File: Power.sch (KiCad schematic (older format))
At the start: 1 part

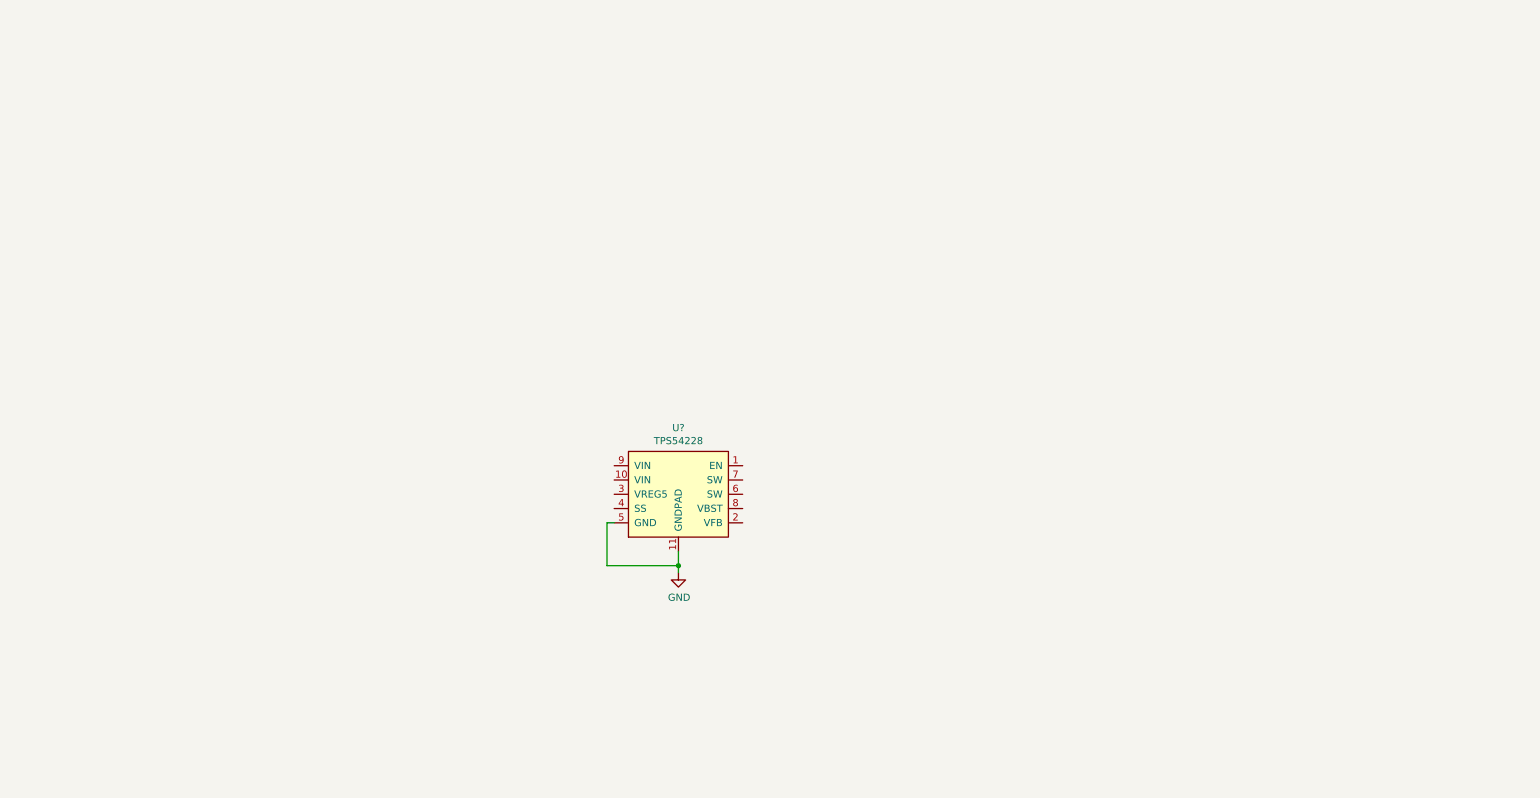
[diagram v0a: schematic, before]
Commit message: Draw power schematic
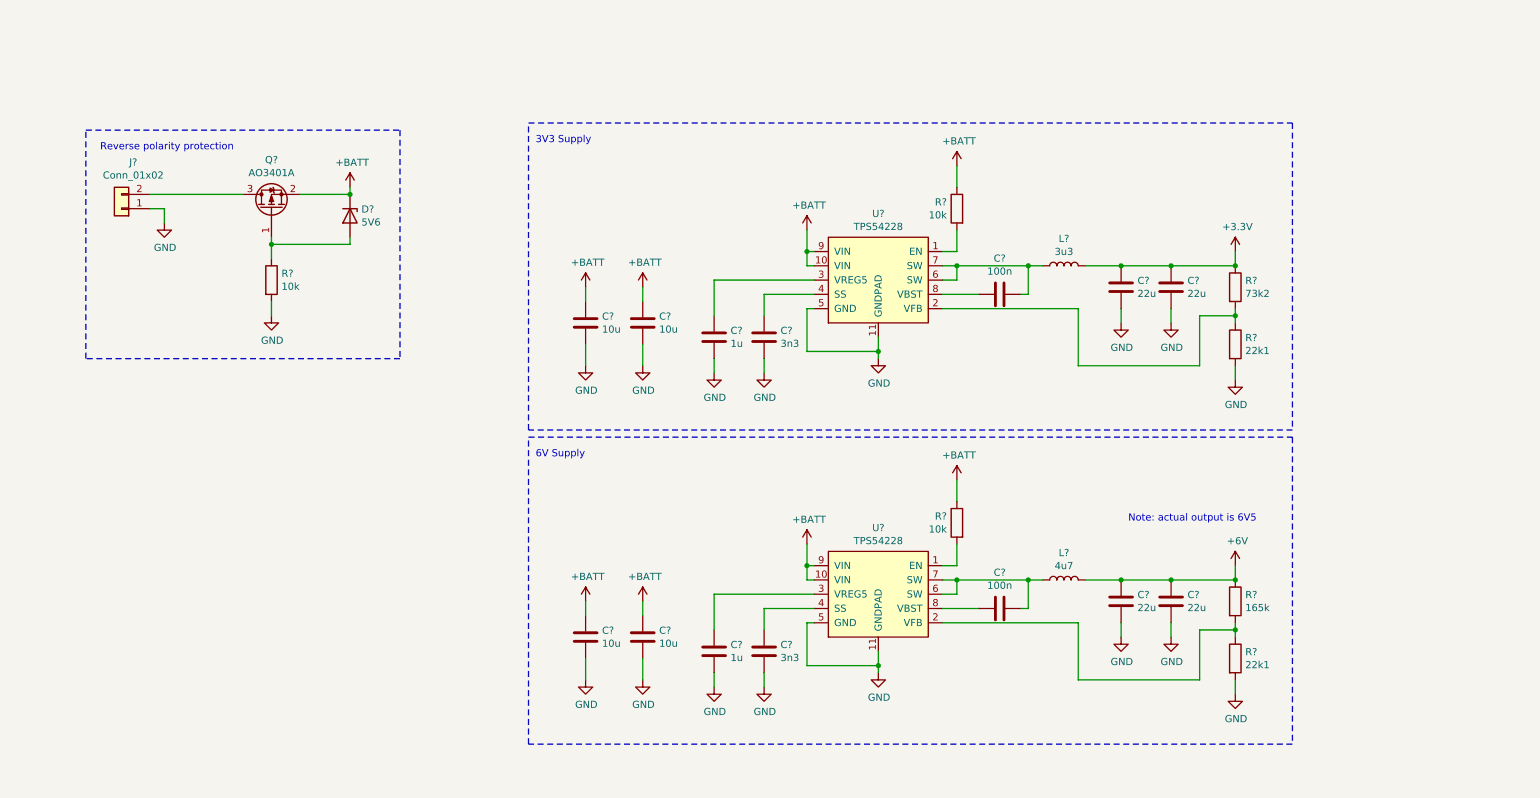
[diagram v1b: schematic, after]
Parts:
- added C? (x2): 1u, symbol Device:C
- added C? (x2): 3n3, symbol Device:C
- added C? (x2): 100n, symbol Device:C
- added C? (x4): 10u, symbol Device:C
- added C? (x4): 22u, symbol Device:C
- added D?: 5V6, symbol Device:D_Zener
- added J?: Conn_01x02, symbol Connector_Generic:Conn_01x02
- added L?: 3u3, symbol Device:L
- added L?: 4u7, symbol Device:L
- added Q?: AO3401A, Package_TO_SOT_SMD:SOT-23, symbol Transistor_FET:AO3401A
- added R? (x3): 10k, symbol Device:R
- added R?: 73k2, symbol Device:R
- added R? (x2): 22k1, symbol Device:R
- added R?: 165k, symbol Device:R
- added U?: TPS54228, symbol co2_sensor_node:TPS54228
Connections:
- net GND: now also C?.2, C?.2, C?.2, C?.2, C?.2, C?.2, C?.2, C?.2, C?.2, C?.2, C?.2, C?.2, J?.1 (Pin_1), R?.2, R?.2, R?.2, U?.11 (GNDPAD), U?.5 (GND)
- net at U?.1 (EN): now also R?.2
- net +BATT: now reaches U?.10 (VIN)
- net +BATT: now also U?.9 (VIN), C?.1, C?.1, C?.1, C?.1, D?.1 (K), Q?.2 (S), R?.1, R?.1, U?.10 (VIN), U?.9 (VIN)
- net at U?.2 (VFB): now also R?.1, R?.2
- net at U?.3 (VREG5): now also C?.1
- net at U?.4 (SS): now also C?.1
- net at U?.6 (SW): now also U?.7 (SW), C?.1, L?.1
- net at U?.8 (VBST): now also C?.2
- new net: R?.2, U?.1 (EN)
- new net: R?.1, R?.2, U?.2 (VFB)
- new net: C?.1, U?.3 (VREG5)
- new net: C?.1, U?.4 (SS)
- new net: C?.1, L?.1, U?.6 (SW), U?.7 (SW)
- new net: C?.2, U?.8 (VBST)
- new net: D?.2 (A), Q?.1 (G), R?.1
- new net: J?.2 (Pin_2), Q?.3 (D)
- new net +3V3: C?.1, C?.1, L?.2, R?.1
- new net +6V: C?.1, C?.1, L?.2, R?.1
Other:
- note added: "3V3 Supply\n"
- note added: "6V Supply\n"
- note added: "Note: actual output is 6V5\n"
- note added: "Reverse polarity protection"
- moved on the sheet: U?

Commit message: Change BME280 out for connector
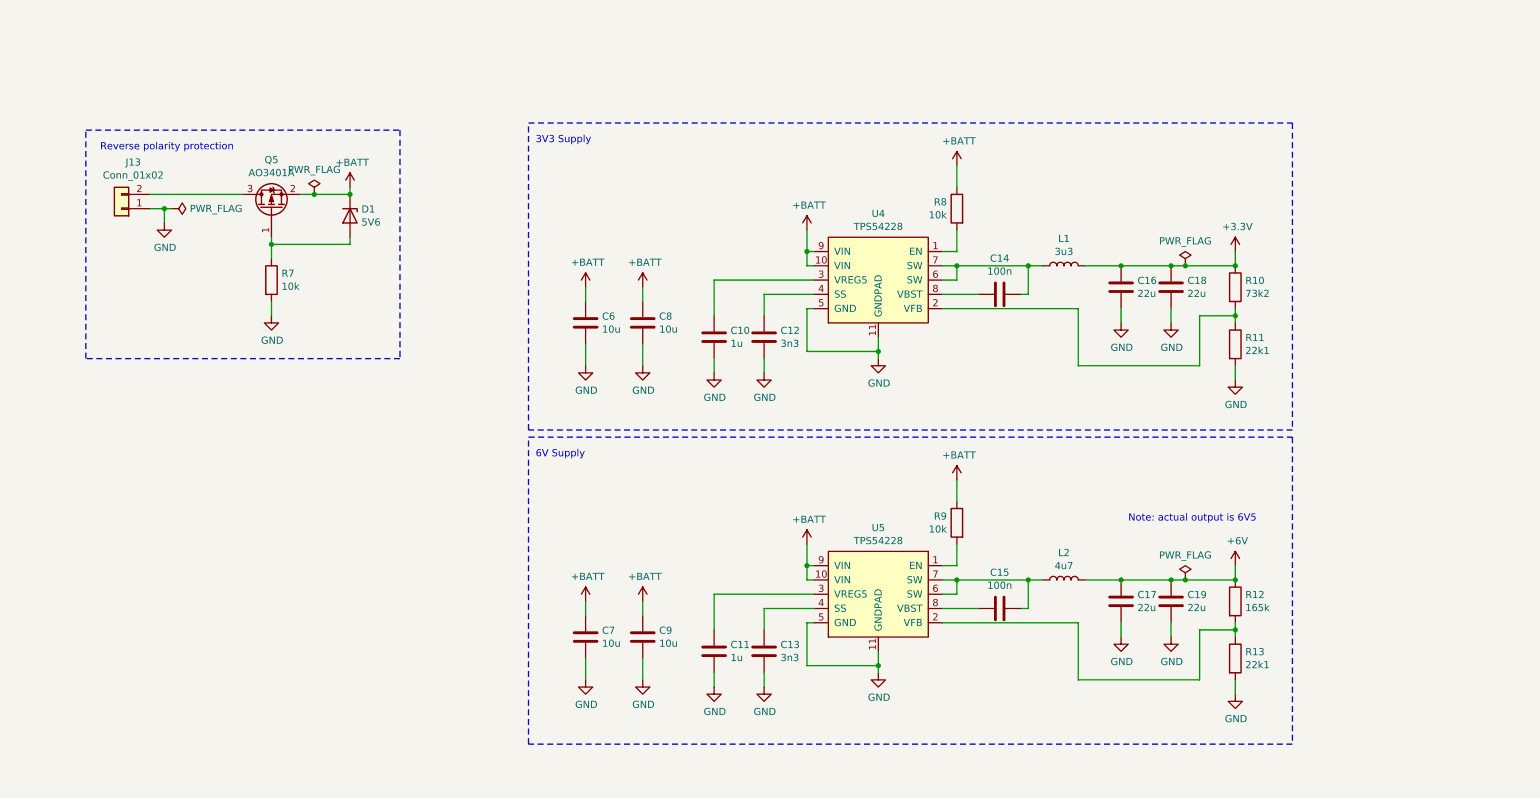
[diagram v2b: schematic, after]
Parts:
- gave numbers to parts that had none: 28

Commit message: Begin assigning footprints
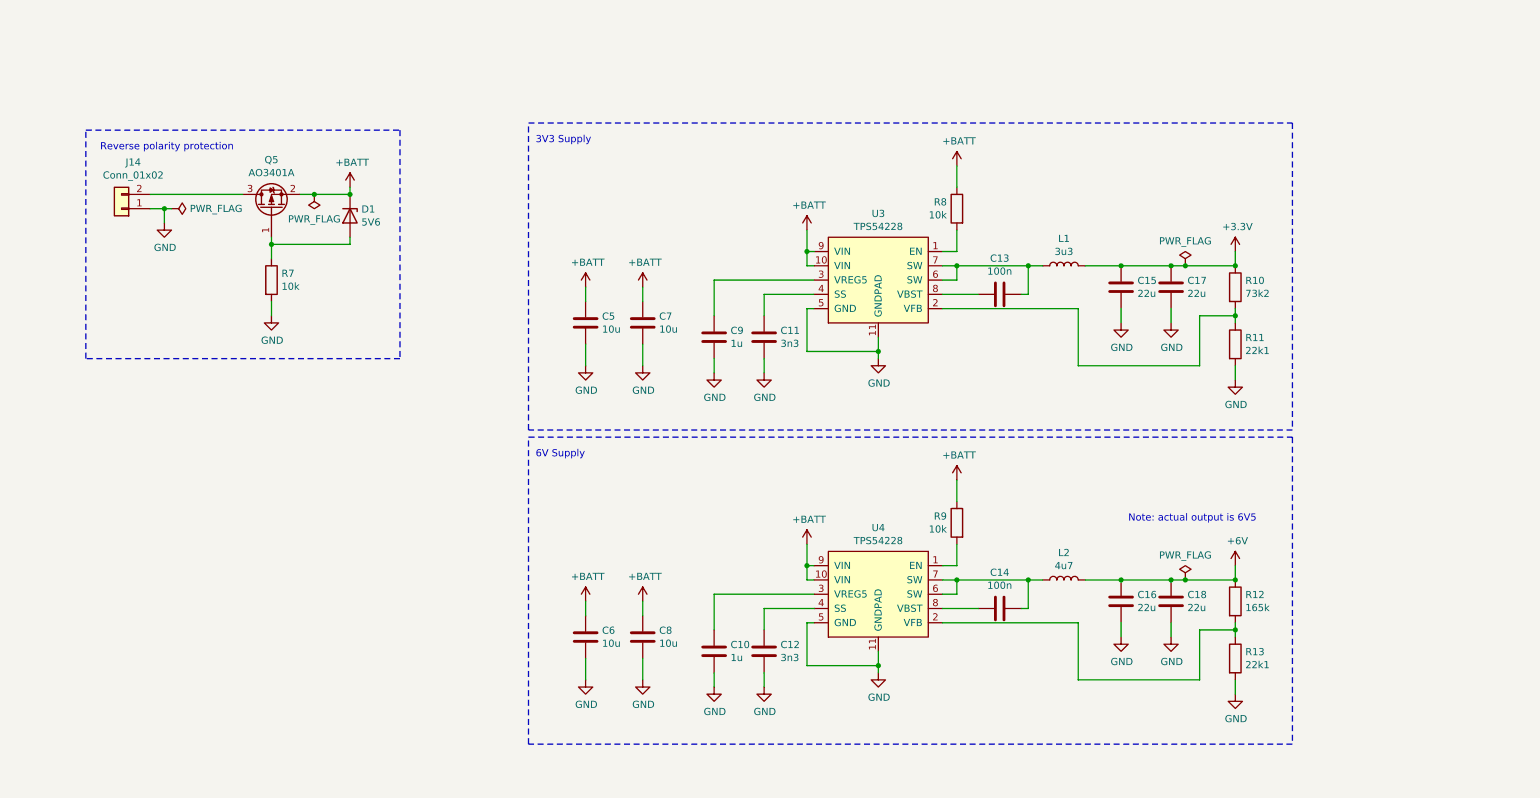
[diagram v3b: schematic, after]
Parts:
- C10: renamed from C11; footprint (none) -> Capacitor_SMD:C_0603_1608Metric; LCSC (none) -> C15849
- C11: renamed from C12; footprint (none) -> Capacitor_SMD:C_0603_1608Metric; LCSC (none) -> C1613
- C12: renamed from C13; footprint (none) -> Capacitor_SMD:C_0603_1608Metric; LCSC (none) -> C1613
- C13: renamed from C14; footprint (none) -> Capacitor_SMD:C_0603_1608Metric; LCSC (none) -> C14663
- C14: renamed from C15; footprint (none) -> Capacitor_SMD:C_0603_1608Metric; LCSC (none) -> C14663
- C15: renamed from C16; footprint (none) -> Capacitor_SMD:C_0805_2012Metric
- C16: renamed from C17; footprint (none) -> Capacitor_SMD:C_0805_2012Metric
- C17: renamed from C18; footprint (none) -> Capacitor_SMD:C_0805_2012Metric
- C18: renamed from C19; footprint (none) -> Capacitor_SMD:C_0805_2012Metric
- C5: renamed from C6; footprint (none) -> Capacitor_SMD:C_0805_2012Metric
- C6: renamed from C7; footprint (none) -> Capacitor_SMD:C_0805_2012Metric
- C7: renamed from C8; footprint (none) -> Capacitor_SMD:C_0805_2012Metric
- C8: renamed from C9; footprint (none) -> Capacitor_SMD:C_0805_2012Metric
- C9: renamed from C10; footprint (none) -> Capacitor_SMD:C_0603_1608Metric; LCSC (none) -> C15849
- D1: footprint (none) -> Diode_SMD:D_MiniMELF
- Q5: LCSC (none) -> C15127
- R10: footprint (none) -> Resistor_SMD:R_0603_1608Metric; LCSC (none) -> C14890
- R11, R13: footprint (none) -> Resistor_SMD:R_0603_1608Metric; LCSC (none) -> C25961
- R12: footprint (none) -> Resistor_SMD:R_0603_1608Metric; LCSC (none) -> C22816
- R7, R8, R9: footprint (none) -> Resistor_SMD:R_0603_1608Metric; LCSC (none) -> C25804
- renumbered J13 to J14, U4 to U3, U5 to U4

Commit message: Finish attaching footprints for revision 1
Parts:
- J14: footprint (none) -> Connector_JST:JST_XH_B2B-XH-AM_1x02_P2.50mm_Vertical
- L1: footprint (none) -> co2_sensor_node:YP0403
- L2: footprint (none) -> co2_sensor_node:WPN4020
- U3, U4: footprint (none) -> Package_SO:SOIC-8_3.9x4.9mm_P1.27mm
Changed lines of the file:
@@
 F 0 "U3" H 6750 3365 50  0000 C CNN
 F 1 "TPS54228" H 6750 3274 50  0000 C CNN
-F 2 "" H 6750 3350 50  0001 C CNN
+F 2 "Package_SO:SOIC-8_3.9x4.9mm_P1.27mm" H 6750 3350 50  0001 C CNN
 F 3 "" H 6750 3350 50  0001 C CNN
 	1    6900 2600
@@
 F 0 "L1" V 8240 2200 50  0000 C CNN
 F 1 "3u3" V 8149 2200 50  0000 C CNN
-F 2 "" H 8050 2200 50  0001 C CNN
-F 3 "~" H 8050 2200 50  0001 C CNN
+F 2 "co2_sensor_node:YP0403" H 8050 2200 50  0001 C CNN
+F 3 "~" H 8050 2200 50  0001 C CIN
 F 4 "C492275" V 8050 2200 50  0001 C CNN "LCSC"
 	1    8050 2200
@@
 F 0 "U4" H 6750 5565 50  0000 C CNN
 F 1 "TPS54228" H 6750 5474 50  0000 C CNN
-F 2 "" H 6750 5550 50  0001 C CNN
+F 2 "Package_SO:SOIC-8_3.9x4.9mm_P1.27mm" H 6750 5550 50  0001 C CNN
 F 3 "" H 6750 5550 50  0001 C CNN
 	1    6900 4800
@@
 F 0 "L2" V 8240 4400 50  0000 C CNN
 F 1 "4u7" V 8149 4400 50  0000 C CNN
-F 2 "" H 8050 4400 50  0001 C CNN
+F 2 "co2_sensor_node:WPN4020" H 8050 4400 50  0001 C CNN
 F 3 "~" H 8050 4400 50  0001 C CNN
 F 4 "C98363" V 8050 4400 50  0001 C CNN "LCSC"
@@
 F 0 "J14" H 1368 1475 50  0000 C CNN
 F 1 "Conn_01x02" H 1368 1566 50  0000 C CNN
-F 2 "" H 1450 1800 50  0001 C CNN
+F 2 "Connector_JST:JST_XH_B2B-XH-AM_1x02_P2.50mm_Vertical" H 1450 1800 50  0001 C CNN
 F 3 "~" H 1450 1800 50  0001 C CNN
 	1    1450 1800

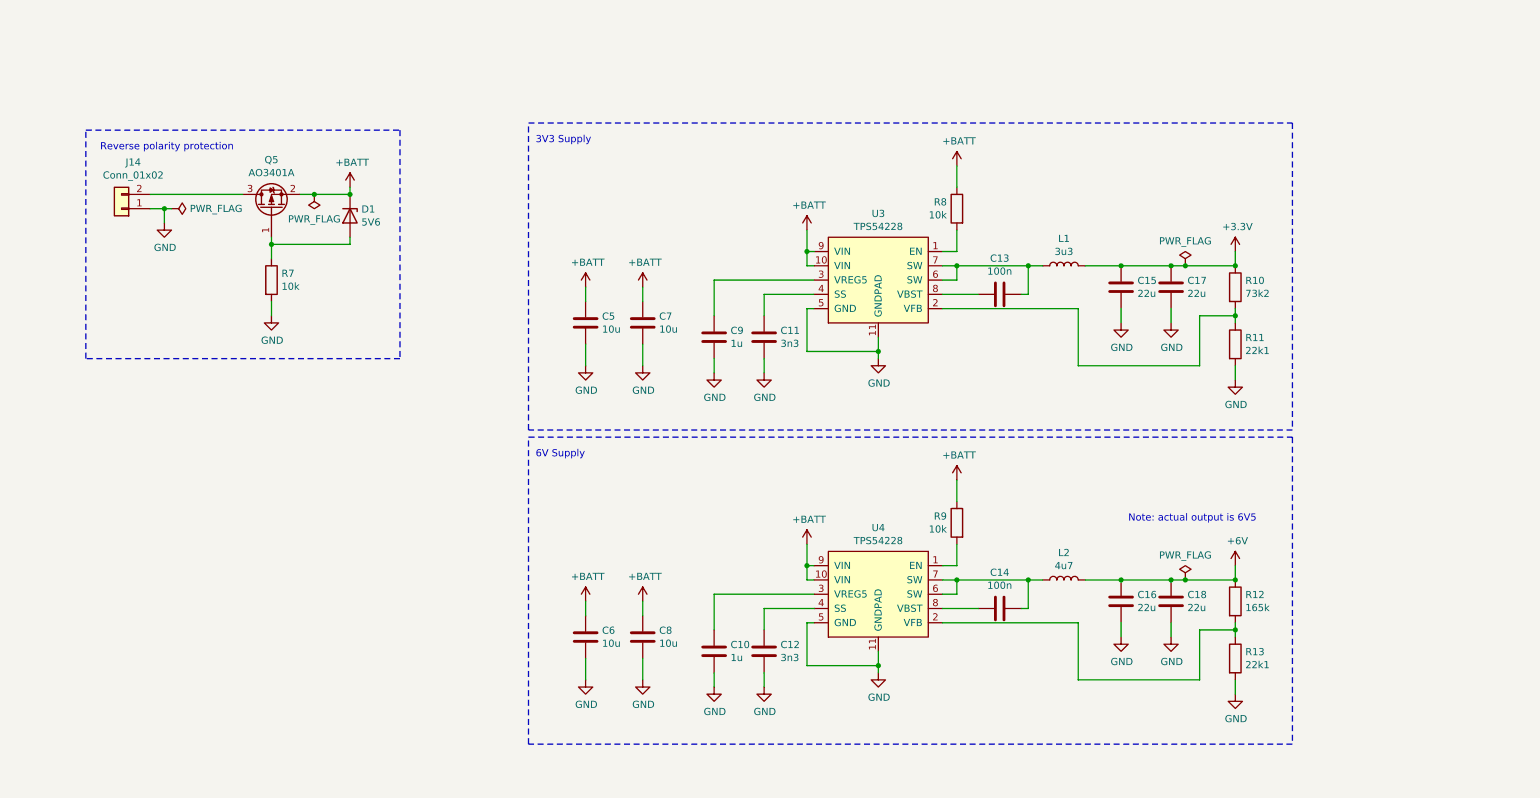
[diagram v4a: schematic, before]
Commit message: Start changing buck converters
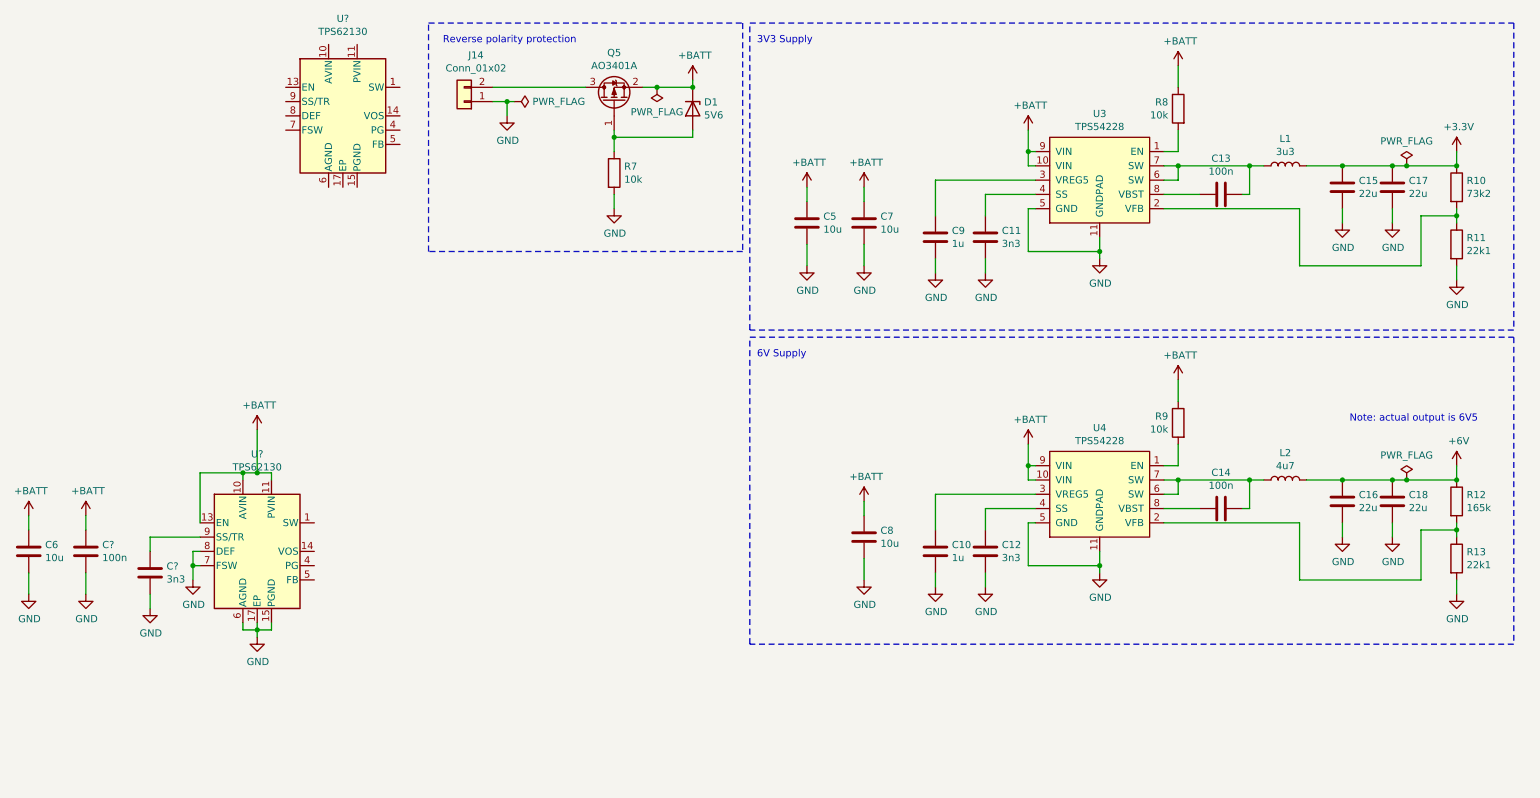
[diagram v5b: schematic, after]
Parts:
- added C?: 100n, symbol Device:C
- added C?: 3n3, symbol Device:C
- added U? (x2): TPS62130, Package_DFN_QFN:VQFN-16-1EP_3x3mm_P0.5mm_EP1.68x1.68mm_ThermalVias, symbol Regulator_Switching:TPS62130
- U3, U4: footprint Package_SO:SOIC-8_3.9x4.9mm_P1.27mm -> Package_SON:VSON-10-1EP_3x3mm_P0.5mm_EP1.2x2mm
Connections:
- net +BATT: now also C?.1, U?.10 (AVIN), U?.11 (PVIN), U?.12 (PVIN), U?.13 (EN)
- net GND: now also C?.2, C?.2, U?.15 (PGND), U?.16 (PGND), U?.17 (EP), U?.6 (AGND), U?.7 (FSW), U?.8 (DEF)
- new net: U?.1 (SW), U?.2 (SW), U?.3 (SW) (x2)
- new net: U?.11 (PVIN), U?.12 (PVIN)
- new net: U?.15 (PGND), U?.16 (PGND)
- new net: C?.1, U?.9 (SS/TR)
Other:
- moved on the sheet: C10, C11, C12, C13, C14, C15, C16, C17, C18, C5, C6, C7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
